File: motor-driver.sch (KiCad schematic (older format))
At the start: 9 parts, among them U3 A3950SLP-T

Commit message: Further work at PCB
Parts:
- R27, R28: footprint Resistor_SMD:R_0805_2012Metric_Pad1.15x1.40mm_HandSolder -> Resistor_SMD:R_0603_1608Metric_Pad1.05x0.95mm_HandSolder
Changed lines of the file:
@@
 AR Path="/5BF2FCBD/5BD9640D" Ref="U?"  Part="1"
 AR Path="/5C015BE4/5BD9640D" Ref="U5"  Part="1"
-F 0 "U3" H 6050 4415 50  0000 C CNN
+F 0 "U5" H 6050 4415 50  0000 C CNN
 F 1 "A3950SLP-T" H 6050 4324 50  0000 C CNN
 F 2 "Package_SO:HTSSOP-16-1EP_4.4x5mm_P0.65mm_EP3.4x5mm_Mask3x3mm_ThermalVias" H 6100 4300 50  0001 C CNN
@@
 AR Path="/5BF2FCBD/5BDA6B35" Ref="C?"  Part="1"
 AR Path="/5C015BE4/5BDA6B35" Ref="C16"  Part="1"
-F 0 "C7" H 6550 4400 50  0000 C CNN
+F 0 "C16" H 6550 4400 50  0000 C CNN
 F 1 "0.1uF 50V" H 6400 4300 50  0000 C CNN
 F 2 "Capacitor_SMD:C_0805_2012Metric_Pad1.15x1.40mm_HandSolder" H 6738 4200 50  0001 C CNN
@@
 AR Path="/5BF2FCBD/5BDBEA6E" Ref="C?"  Part="1"
 AR Path="/5C015BE4/5BDBEA6E" Ref="C20"  Part="1"
-F 0 "C11" V 7200 3750 50  0000 L CNN
+F 0 "C20" V 7200 3750 50  0000 L CNN
 F 1 "0.1uF 50V" V 7100 3600 50  0000 L CNN
 F 2 "Capacitor_SMD:C_0805_2012Metric_Pad1.15x1.40mm_HandSolder" H 7388 3650 50  0001 C CNN
@@
 AR Path="/5BF2FCBD/5BDD7CCD" Ref="C?"  Part="1"
 AR Path="/5C015BE4/5BDD7CCD" Ref="C17"  Part="1"
-F 0 "C8" V 6550 3350 50  0000 C CNN
+F 0 "C17" V 6550 3350 50  0000 C CNN
 F 1 "0.1uF 50V" V 6650 3350 50  0000 C CNN
 F 2 "Capacitor_SMD:C_0805_2012Metric_Pad1.15x1.40mm_HandSolder" H 6888 3200 50  0001 C CNN
@@
 AR Path="/5BF2FCBD/5BDE6995" Ref="C?"  Part="1"
 AR Path="/5C015BE4/5BDE6995" Ref="C18"  Part="1"
-F 0 "C9" H 7218 4396 50  0000 L CNN
+F 0 "C18" H 7218 4396 50  0000 L CNN
 F 1 "100uF" H 7218 4305 50  0000 L CNN
 F 2 "Capacitor_SMD:CP_Elec_8x10.5" H 7138 4200 50  0001 C CNN
@@
 AR Path="/5BF2FCBD/5BDFF4AF" Ref="C?"  Part="1"
 AR Path="/5C015BE4/5BDFF4AF" Ref="C19"  Part="1"
-F 0 "C10" V 7098 3200 50  0000 C CNN
+F 0 "C19" V 7098 3200 50  0000 C CNN
 F 1 "0.22uF 25V" V 7189 3200 50  0000 C CNN
 F 2 "Capacitor_SMD:C_0603_1608Metric_Pad1.05x0.95mm_HandSolder" H 7388 3050 50  0001 C CNN
@@
 AR Path="/5BF2FCBD/5BE2A012" Ref="R?"  Part="1"
 AR Path="/5C015BE4/5BE2A012" Ref="R44"  Part="1"
-F 0 "R27" H 5070 2846 50  0000 L CNN
+F 0 "R44" H 5070 2846 50  0000 L CNN
 F 1 "5k" H 5070 2755 50  0000 L CNN
-F 2 "Resistor_SMD:R_0805_2012Metric_Pad1.15x1.40mm_HandSolder" V 4930 2800 50  0001 C CNN
+F 2 "Resistor_SMD:R_0603_1608Metric_Pad1.05x0.95mm_HandSolder" V 4930 2800 50  0001 C CNN
 F 3 "~" H 5000 2800 50  0001 C CNN
 	1    5000 2800
@@
 AR Path="/5BF2FCBD/5BE427B2" Ref="D?"  Part="1"
 AR Path="/5C015BE4/5BE427B2" Ref="D8"  Part="1"
-F 0 "D5" V 5438 2282 50  0000 R CNN
+F 0 "D8" V 5438 2282 50  0000 R CNN
 F 1 "RED" V 5347 2282 50  0000 R CNN
 F 2 "LED_SMD:LED_0603_1608Metric_Pad1.05x0.95mm_HandSolder" H 5400 2400 50  0001 C CNN
@@
 AR Path="/5BF2FCBD/5BE42954" Ref="R?"  Part="1"
 AR Path="/5C015BE4/5BE42954" Ref="R45"  Part="1"
-F 0 "R28" H 5470 2846 50  0000 L CNN
+F 0 "R45" H 5470 2846 50  0000 L CNN
 F 1 "220" H 5470 2755 50  0000 L CNN
-F 2 "Resistor_SMD:R_0805_2012Metric_Pad1.15x1.40mm_HandSolder" V 5330 2800 50  0001 C CNN
+F 2 "Resistor_SMD:R_0603_1608Metric_Pad1.05x0.95mm_HandSolder" V 5330 2800 50  0001 C CNN
 F 3 "~" H 5400 2800 50  0001 C CNN
 	1    5400 2800

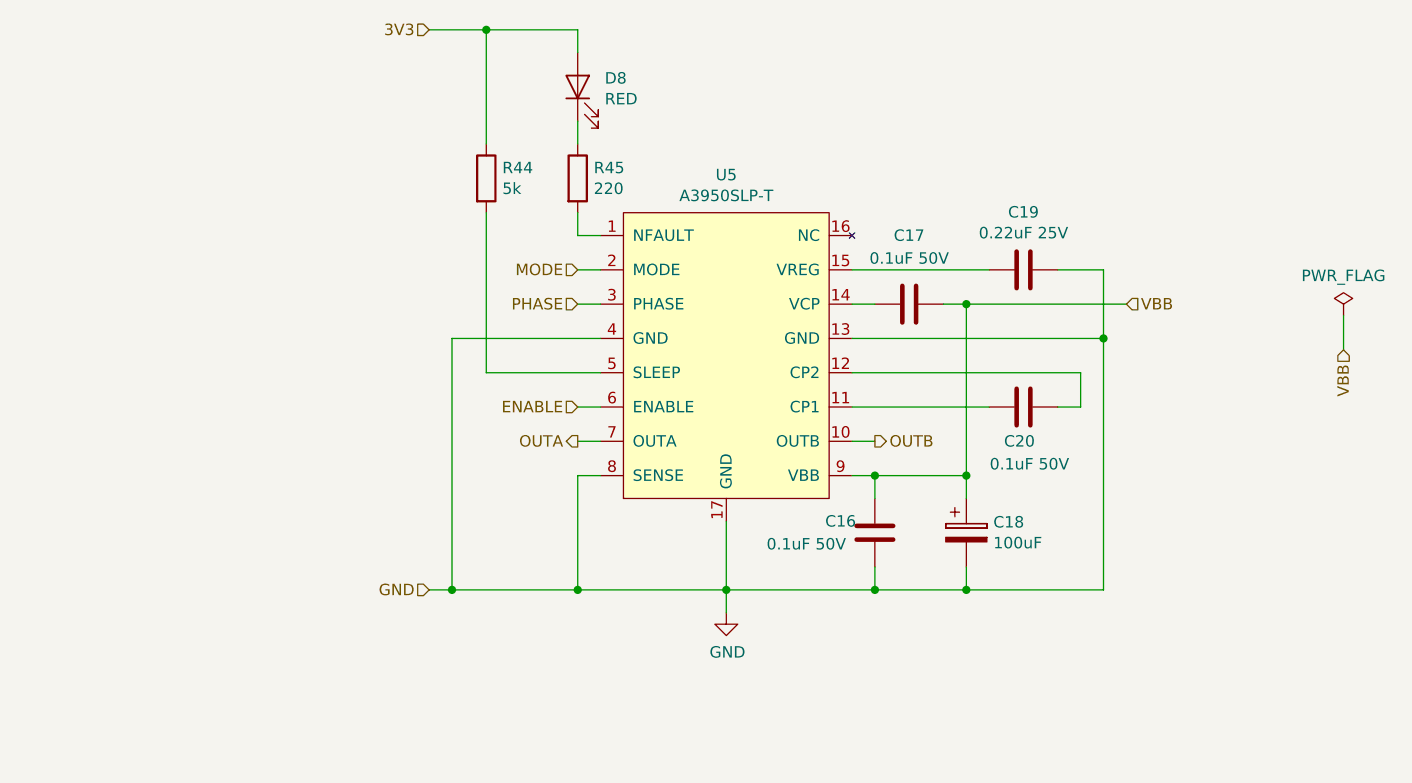
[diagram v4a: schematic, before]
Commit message: Changed Motor Controller to DRV8840, removed pre-motor power section. Replaced PNP transistors in logic level shifters with P-MOSFET units
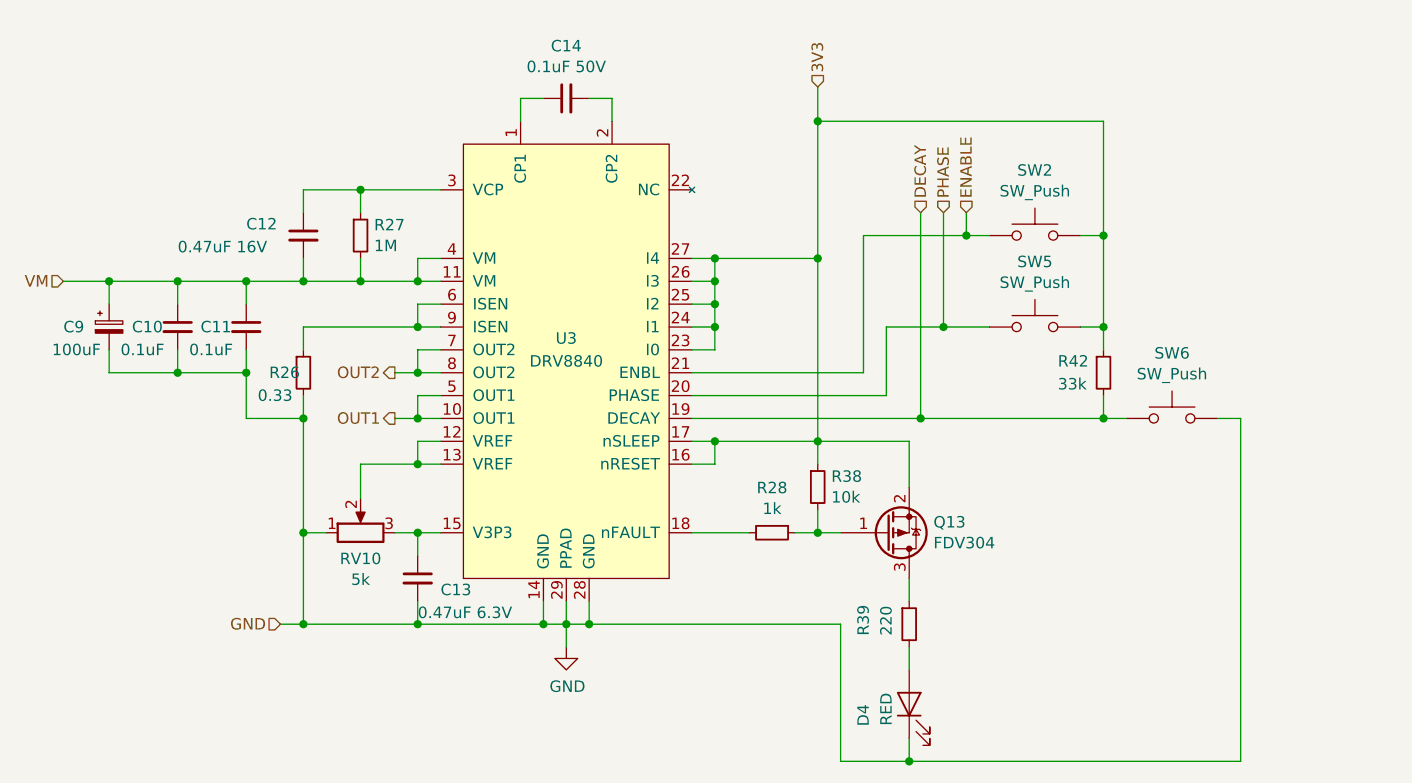
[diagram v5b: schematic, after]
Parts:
- removed C10: 0.22uF 25V, Capacitor_SMD:C_0603_1608Metric_Pad1.05x0.95mm_HandSolder, symbol Device:C
- removed C11, C7, C8: 0.1uF 50V, Capacitor_SMD:C_0805_2012Metric_Pad1.15x1.40mm_HandSolder, symbol Device:C
- removed C9: 100uF, Capacitor_SMD:CP_Elec_8x10.5, symbol Device:CP
- removed D5: RED, LED_SMD:LED_0603_1608Metric_Pad1.05x0.95mm_HandSolder, symbol Device:LED
- removed R27: 5k, Resistor_SMD:R_0603_1608Metric_Pad1.05x0.95mm_HandSolder, symbol Device:R
- removed R28: 220, Resistor_SMD:R_0603_1608Metric_Pad1.05x0.95mm_HandSolder, symbol Device:R
- removed U3: A3950SLP-T, Package_SO:HTSSOP-16-1EP_4.4x5mm_P0.65mm_EP3.4x5mm_Mask3x3mm_ThermalVias, symbol mylib:A3950SLP-T
- added C3: 100uF, Capacitor_SMD:CP_Elec_6.3x7.7, symbol Device:CP_Small
- added C4, C5: 0.1uF, Capacitor_SMD:C_0603_1608Metric, symbol Device:C_Small
- added C6: 0.47uF 16V, Capacitor_SMD:C_0603_1608Metric, symbol Device:C_Small
- added C7: 0.47uF 6.3V, Capacitor_SMD:C_0603_1608Metric, symbol Device:C_Small
- added C8: 0.1uF 50V, Capacitor_SMD:C_0603_1608Metric, symbol Device:C_Small
- added D3: RED, LED_SMD:LED_0603_1608Metric_Castellated, symbol Device:LED
- added Q13: FDV304, Package_TO_SOT_SMD:SOT-23, symbol Device:Q_PMOS_GSD
- added R21: 0.33, Resistor_SMD:R_2512_6332Metric, symbol Device:R_Small
- added R22: 1M, Resistor_SMD:R_0603_1608Metric, symbol Device:R_Small
- added R23: 1k, Resistor_SMD:R_0603_1608Metric, symbol Device:R_Small
- added R24: 10k, Resistor_SMD:R_0603_1608Metric, symbol Device:R_Small
- added R25: 220, Resistor_SMD:R_0603_1608Metric, symbol Device:R_Small
- added R41: 33k, Resistor_SMD:R_0603_1608Metric, symbol Device:R_Small
- added RV1: 5k, Potentiometer_THT:Potentiometer_Bourns_3266W_Vertical, symbol Device:R_POT
- added SW1, SW3, SW4: SW_Push, Button_Switch_SMD:SW_SPST_KMR2, symbol Switch:SW_Push
- added U2: DRV8840, SOP65P640X110-29N:SOP65P640X110-29N, symbol mylib:DRV8840
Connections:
- net 3V3: now also Q13.2 (S), R24.1, R41.1, SW1.2, SW3.2, U2.16 (nRESET), U2.17 (nSLEEP), U2.23 (I0), U2.24 (I1), U2.25 (I2), U2.26 (I3), U2.27 (I4)
- net ENABLE: now also SW1.1, U2.21 (ENBL)
- net GND: now also C3.2, C4.2, C5.2, C7.2, D3.1 (K), R21.2, RV1.1, SW4.2, U2.14 (GND), U2.28 (GND), U2.29 (PPAD)
- net PHASE: now also SW3.1, U2.20 (PHASE)
- new net: C8.1, U2.1 (CP1)
- new net: RV1.2, U2.12 (VREF), U2.13 (VREF)
- new net: C7.1, RV1.3, U2.15 (V3P3)
- new net: R23.2, U2.18 (nFAULT)
- new net: C8.2, U2.2 (CP2)
- new net: C6.1, R22.1, U2.3 (VCP)
- new net: R21.1, U2.6 (ISEN), U2.9 (ISEN)
- new net: Q13.1 (G), R23.1, R24.2
- new net: D3.2 (A), R25.2
- new net: Q13.3 (D), R25.1
- new net DECAY: R41.2, SW4.1, U2.19 (DECAY)
- new net OUT1: U2.10 (OUT1), U2.5 (OUT1)
- new net OUT2: U2.7 (OUT2), U2.8 (OUT2)
- new net VM: C3.1, C4.1, C5.1, C6.2, R22.2, U2.11 (VM), U2.4 (VM)

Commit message: Re-placed components of 3.3->24V converter. Improvement placement of Motor Controller components
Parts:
- C3: footprint Capacitor_SMD:CP_Elec_6.3x7.7 -> Capacitor_THT:CP_Radial_D6.3mm_P2.50mm
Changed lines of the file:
@@
 F 0 "C9" H 3150 3450 50  0000 L CNN
 F 1 "100uF" H 3100 3350 50  0000 L CNN
-F 2 "Capacitor_SMD:CP_Elec_6.3x7.7" H 3350 3450 50  0001 C CNN
+F 2 "Capacitor_THT:CP_Radial_D6.3mm_P2.50mm" H 3350 3450 50  0001 C CNN
 F 3 "~" H 3350 3450 50  0001 C CNN
 	1    3350 3450

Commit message: Routed all nets without GND. Added logo
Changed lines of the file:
@@
 $Descr A4 11693 8268
 encoding utf-8
-Sheet 7 8
+Sheet 5 8
 Title ""
 Date ""
@@
 AR Path="/5BDB64FF/5BE79BC7" Ref="R22"  Part="1"
 AR Path="/5C015BE4/5BE79BC7" Ref="R27"  Part="1"
-F 0 "R27" H 4509 3096 50  0000 L CNN
+F 0 "R22" H 4509 3096 50  0000 L CNN
 F 1 "1M" H 4509 3005 50  0000 L CNN
 F 2 "Resistor_SMD:R_0603_1608Metric" H 4450 3050 50  0001 C CNN
@@
 AR Path="/5BDB64FF/5BE79D59" Ref="C8"  Part="1"
 AR Path="/5C015BE4/5BE79D59" Ref="C14"  Part="1"
-F 0 "C14" V 5579 2450 50  0000 C CNN
+F 0 "C8" V 5579 2450 50  0000 C CNN
 F 1 "0.1uF 50V" V 5488 2450 50  0000 C CNN
 F 2 "Capacitor_SMD:C_0603_1608Metric" H 5350 2450 50  0001 C CNN
@@
 AR Path="/5BDB64FF/5BE7C590" Ref="C6"  Part="1"
 AR Path="/5C015BE4/5BE7C590" Ref="C12"  Part="1"
-F 0 "C12" H 3950 3100 50  0000 L CNN
+F 0 "C6" H 3950 3100 50  0000 L CNN
 F 1 "0.47uF 16V" H 3650 3000 50  0000 L CNN
 F 2 "Capacitor_SMD:C_0603_1608Metric" H 4200 3050 50  0001 C CNN
@@
 AR Path="/5BDB64FF/5BE78B4F" Ref="U2"  Part="1"
 AR Path="/5C015BE4/5BE78B4F" Ref="U3"  Part="1"
-F 0 "U3" H 5350 3700 50  0000 C CNN
+F 0 "U2" H 5350 3700 50  0000 C CNN
 F 1 "DRV8840" H 5350 3600 50  0000 C CNN
 F 2 "SOP65P640X110-29N:SOP65P640X110-29N" H 5200 3700 50  0001 C CNN
@@
 AR Path="/5BDB64FF/5BE7DEED" Ref="C5"  Part="1"
 AR Path="/5C015BE4/5BE7DEED" Ref="C11"  Part="1"
-F 0 "C11" H 3750 3450 50  0000 L CNN
+F 0 "C5" H 3750 3450 50  0000 L CNN
 F 1 "0.1uF" H 3700 3350 50  0000 L CNN
 F 2 "Capacitor_SMD:C_0603_1608Metric" H 3950 3450 50  0001 C CNN
@@
 AR Path="/5BDB64FF/5BE7DF37" Ref="C4"  Part="1"
 AR Path="/5C015BE4/5BE7DF37" Ref="C10"  Part="1"
-F 0 "C10" H 3450 3450 50  0000 L CNN
+F 0 "C4" H 3450 3450 50  0000 L CNN
 F 1 "0.1uF" H 3400 3350 50  0000 L CNN
 F 2 "Capacitor_SMD:C_0603_1608Metric" H 3650 3450 50  0001 C CNN
@@
 AR Path="/5BDB64FF/5BE7EFAF" Ref="C3"  Part="1"
 AR Path="/5C015BE4/5BE7EFAF" Ref="C9"  Part="1"
-F 0 "C9" H 3150 3450 50  0000 L CNN
+F 0 "C3" H 3150 3450 50  0000 L CNN
 F 1 "100uF" H 3100 3350 50  0000 L CNN
 F 2 "Capacitor_THT:CP_Radial_D6.3mm_P2.50mm" H 3350 3450 50  0001 C CNN
@@
 AR Path="/5BDB64FF/5BE7F85E" Ref="#PWR05"  Part="1"
 AR Path="/5C015BE4/5BE7F85E" Ref="#PWR07"  Part="1"
-F 0 "#PWR07" H 5350 4600 50  0001 C CNN
+F 0 "#PWR05" H 5350 4600 50  0001 C CNN
 F 1 "GND" H 5355 4677 50  0000 C CNN
 F 2 "" H 5350 4850 50  0001 C CNN
@@
 AR Path="/5BDB64FF/5BE84287" Ref="R21"  Part="1"
 AR Path="/5C015BE4/5BE84287" Ref="R26"  Part="1"
-F 0 "R26" H 4050 3650 50  0000 L CNN
+F 0 "R21" H 4050 3650 50  0000 L CNN
 F 1 "0.33" H 4000 3550 50  0000 L CNN
 F 2 "Resistor_SMD:R_2512_6332Metric" H 4200 3650 50  0001 C CNN
@@
 AR Path="/5BDB64FF/5BEAA7B3" Ref="R24"  Part="1"
 AR Path="/5C015BE4/5BEAA7B3" Ref="R38"  Part="1"
-F 0 "R38" H 6509 4196 50  0000 L CNN
+F 0 "R24" H 6509 4196 50  0000 L CNN
 F 1 "10k" H 6509 4105 50  0000 L CNN
 F 2 "Resistor_SMD:R_0603_1608Metric" H 6450 4150 50  0001 C CNN
@@
 AR Path="/5BDB64FF/5BEAD7B9" Ref="R23"  Part="1"
 AR Path="/5C015BE4/5BEAD7B9" Ref="R28"  Part="1"
-F 0 "R28" V 6054 4350 50  0000 C CNN
+F 0 "R23" V 6054 4350 50  0000 C CNN
 F 1 "1k" V 6145 4350 50  0000 C CNN
 F 2 "Resistor_SMD:R_0603_1608Metric" H 6250 4350 50  0001 C CNN
@@
 AR Path="/5BDB64FF/5BEB256D" Ref="D3"  Part="1"
 AR Path="/5C015BE4/5BEB256D" Ref="D4"  Part="1"
-F 0 "D4" H 6850 5300 50  0000 R CNN
+F 0 "D3" H 6850 5300 50  0000 R CNN
 F 1 "RED" H 6900 5200 50  0000 R CNN
 F 2 "LED_SMD:LED_0603_1608Metric_Castellated" H 6850 5100 50  0001 C CNN
@@
 AR Path="/5BDB64FF/5BEB7620" Ref="R25"  Part="1"
 AR Path="/5C015BE4/5BEB7620" Ref="R39"  Part="1"
-F 0 "R39" V 6650 4700 50  0000 L CNN
+F 0 "R25" V 6650 4700 50  0000 L CNN
 F 1 "220" V 6750 4700 50  0000 L CNN
 F 2 "Resistor_SMD:R_0603_1608Metric" H 6850 4750 50  0001 C CNN
@@
 AR Path="/5BDB64FF/5BECAFEA" Ref="C7"  Part="1"
 AR Path="/5C015BE4/5BECAFEA" Ref="C13"  Part="1"
-F 0 "C13" H 4800 4500 50  0000 L CNN
+F 0 "C7" H 4800 4500 50  0000 L CNN
 F 1 "0.47uF 6.3V" H 4700 4400 50  0000 L CNN
 F 2 "Capacitor_SMD:C_0603_1608Metric" H 4700 4550 50  0001 C CNN
@@
 AR Path="/5BDB64FF/5BE92513" Ref="RV1"  Part="1"
 AR Path="/5C015BE4/5BE92513" Ref="RV10"  Part="1"
-F 0 "RV10" V 4336 4350 50  0000 C CNN
+F 0 "RV1" V 4336 4350 50  0000 C CNN
 F 1 "5k" V 4245 4350 50  0000 C CNN
 F 2 "Potentiometer_THT:Potentiometer_Bourns_3266W_Vertical" H 4450 4350 50  0001 C CNN
@@
 AR Path="/5C015BE4/5BF252CB" Ref="Q13"  Part="1"
 AR Path="/5BDB64FF/5BF252CB" Ref="Q9"  Part="1"
-F 0 "Q13" H 6956 4304 50  0000 L CNN
+F 0 "Q9" H 6956 4304 50  0000 L CNN
 F 1 "FDV304" H 6956 4395 50  0000 L CNN
 F 2 "Package_TO_SOT_SMD:SOT-23" H 6950 4450 50  0001 C CNN
@@
 AR Path="/5BDB64FF/5BE949DE" Ref="SW1"  Part="1"
 AR Path="/5C015BE4/5BE949DE" Ref="SW2"  Part="1"
-F 0 "SW2" H 7400 3335 50  0000 C CNN
+F 0 "SW1" H 7400 3335 50  0000 C CNN
 F 1 "SW_Push" H 7400 3244 50  0000 C CNN
 F 2 "Button_Switch_SMD:SW_SPST_KMR2" H 7400 3250 50  0001 C CNN
@@
 AR Path="/5BDB64FF/5BE950B7" Ref="SW3"  Part="1"
 AR Path="/5C015BE4/5BE950B7" Ref="SW5"  Part="1"
-F 0 "SW5" H 7400 3735 50  0000 C CNN
+F 0 "SW3" H 7400 3735 50  0000 C CNN
 F 1 "SW_Push" H 7400 3644 50  0000 C CNN
 F 2 "Button_Switch_SMD:SW_SPST_KMR2" H 7400 3650 50  0001 C CNN
@@
 AR Path="/5BDB64FF/5BE950FD" Ref="SW4"  Part="1"
 AR Path="/5C015BE4/5BE950FD" Ref="SW6"  Part="1"
-F 0 "SW6" H 8000 4135 50  0000 C CNN
+F 0 "SW4" H 8000 4135 50  0000 C CNN
 F 1 "SW_Push" H 8000 4044 50  0000 C CNN
 F 2 "Button_Switch_SMD:SW_SPST_KMR2" H 8000 4050 50  0001 C CNN
@@
 AR Path="/5BDB64FF/5BEB4B1E" Ref="R41"  Part="1"
 AR Path="/5C015BE4/5BEB4B1E" Ref="R42"  Part="1"
-F 0 "R42" H 7500 3700 50  0000 L CNN
+F 0 "R41" H 7500 3700 50  0000 L CNN
 F 1 "33k" H 7500 3600 50  0000 L CNN
 F 2 "Resistor_SMD:R_0603_1608Metric" H 7700 3650 50  0001 C CNN

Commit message: Added switch for selecting Low/High power motor. Added thermal pads around motor controllers.
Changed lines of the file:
@@
 $Descr A4 11693 8268
 encoding utf-8
-Sheet 5 8
+Sheet 7 8
 Title ""
 Date ""
@@
 AR Path="/5BDB64FF/5BE79BC7" Ref="R22"  Part="1"
 AR Path="/5C015BE4/5BE79BC7" Ref="R27"  Part="1"
-F 0 "R22" H 4509 3096 50  0000 L CNN
+F 0 "R27" H 4509 3096 50  0000 L CNN
 F 1 "1M" H 4509 3005 50  0000 L CNN
 F 2 "Resistor_SMD:R_0603_1608Metric" H 4450 3050 50  0001 C CNN
@@
 AR Path="/5BDB64FF/5BE79D59" Ref="C8"  Part="1"
 AR Path="/5C015BE4/5BE79D59" Ref="C14"  Part="1"
-F 0 "C8" V 5579 2450 50  0000 C CNN
+F 0 "C14" V 5579 2450 50  0000 C CNN
 F 1 "0.1uF 50V" V 5488 2450 50  0000 C CNN
 F 2 "Capacitor_SMD:C_0603_1608Metric" H 5350 2450 50  0001 C CNN
@@
 AR Path="/5BDB64FF/5BE7C590" Ref="C6"  Part="1"
 AR Path="/5C015BE4/5BE7C590" Ref="C12"  Part="1"
-F 0 "C6" H 3950 3100 50  0000 L CNN
+F 0 "C12" H 3950 3100 50  0000 L CNN
 F 1 "0.47uF 16V" H 3650 3000 50  0000 L CNN
 F 2 "Capacitor_SMD:C_0603_1608Metric" H 4200 3050 50  0001 C CNN
@@
 AR Path="/5BDB64FF/5BE78B4F" Ref="U2"  Part="1"
 AR Path="/5C015BE4/5BE78B4F" Ref="U3"  Part="1"
-F 0 "U2" H 5350 3700 50  0000 C CNN
+F 0 "U3" H 5350 3700 50  0000 C CNN
 F 1 "DRV8840" H 5350 3600 50  0000 C CNN
 F 2 "SOP65P640X110-29N:SOP65P640X110-29N" H 5200 3700 50  0001 C CNN
@@
 AR Path="/5BDB64FF/5BE7DEED" Ref="C5"  Part="1"
 AR Path="/5C015BE4/5BE7DEED" Ref="C11"  Part="1"
-F 0 "C5" H 3750 3450 50  0000 L CNN
+F 0 "C11" H 3750 3450 50  0000 L CNN
 F 1 "0.1uF" H 3700 3350 50  0000 L CNN
 F 2 "Capacitor_SMD:C_0603_1608Metric" H 3950 3450 50  0001 C CNN
@@
 AR Path="/5BDB64FF/5BE7DF37" Ref="C4"  Part="1"
 AR Path="/5C015BE4/5BE7DF37" Ref="C10"  Part="1"
-F 0 "C4" H 3450 3450 50  0000 L CNN
+F 0 "C10" H 3450 3450 50  0000 L CNN
 F 1 "0.1uF" H 3400 3350 50  0000 L CNN
 F 2 "Capacitor_SMD:C_0603_1608Metric" H 3650 3450 50  0001 C CNN
@@
 AR Path="/5BDB64FF/5BE7EFAF" Ref="C3"  Part="1"
 AR Path="/5C015BE4/5BE7EFAF" Ref="C9"  Part="1"
-F 0 "C3" H 3150 3450 50  0000 L CNN
+F 0 "C9" H 3150 3450 50  0000 L CNN
 F 1 "100uF" H 3100 3350 50  0000 L CNN
 F 2 "Capacitor_THT:CP_Radial_D6.3mm_P2.50mm" H 3350 3450 50  0001 C CNN
@@
 AR Path="/5BDB64FF/5BE7F85E" Ref="#PWR05"  Part="1"
 AR Path="/5C015BE4/5BE7F85E" Ref="#PWR07"  Part="1"
-F 0 "#PWR05" H 5350 4600 50  0001 C CNN
+F 0 "#PWR07" H 5350 4600 50  0001 C CNN
 F 1 "GND" H 5355 4677 50  0000 C CNN
 F 2 "" H 5350 4850 50  0001 C CNN
@@
 AR Path="/5BDB64FF/5BE84287" Ref="R21"  Part="1"
 AR Path="/5C015BE4/5BE84287" Ref="R26"  Part="1"
-F 0 "R21" H 4050 3650 50  0000 L CNN
+F 0 "R26" H 4050 3650 50  0000 L CNN
 F 1 "0.33" H 4000 3550 50  0000 L CNN
 F 2 "Resistor_SMD:R_2512_6332Metric" H 4200 3650 50  0001 C CNN
@@
 AR Path="/5BDB64FF/5BEAA7B3" Ref="R24"  Part="1"
 AR Path="/5C015BE4/5BEAA7B3" Ref="R38"  Part="1"
-F 0 "R24" H 6509 4196 50  0000 L CNN
+F 0 "R38" H 6509 4196 50  0000 L CNN
 F 1 "10k" H 6509 4105 50  0000 L CNN
 F 2 "Resistor_SMD:R_0603_1608Metric" H 6450 4150 50  0001 C CNN
@@
 AR Path="/5BDB64FF/5BEAD7B9" Ref="R23"  Part="1"
 AR Path="/5C015BE4/5BEAD7B9" Ref="R28"  Part="1"
-F 0 "R23" V 6054 4350 50  0000 C CNN
+F 0 "R28" V 6054 4350 50  0000 C CNN
 F 1 "1k" V 6145 4350 50  0000 C CNN
 F 2 "Resistor_SMD:R_0603_1608Metric" H 6250 4350 50  0001 C CNN
@@
 AR Path="/5BDB64FF/5BEB256D" Ref="D3"  Part="1"
 AR Path="/5C015BE4/5BEB256D" Ref="D4"  Part="1"
-F 0 "D3" H 6850 5300 50  0000 R CNN
+F 0 "D4" H 6850 5300 50  0000 R CNN
 F 1 "RED" H 6900 5200 50  0000 R CNN
 F 2 "LED_SMD:LED_0603_1608Metric_Castellated" H 6850 5100 50  0001 C CNN
@@
 AR Path="/5BDB64FF/5BEB7620" Ref="R25"  Part="1"
 AR Path="/5C015BE4/5BEB7620" Ref="R39"  Part="1"
-F 0 "R25" V 6650 4700 50  0000 L CNN
+F 0 "R39" V 6650 4700 50  0000 L CNN
 F 1 "220" V 6750 4700 50  0000 L CNN
 F 2 "Resistor_SMD:R_0603_1608Metric" H 6850 4750 50  0001 C CNN
@@
 AR Path="/5BDB64FF/5BECAFEA" Ref="C7"  Part="1"
 AR Path="/5C015BE4/5BECAFEA" Ref="C13"  Part="1"
-F 0 "C7" H 4800 4500 50  0000 L CNN
+F 0 "C13" H 4800 4500 50  0000 L CNN
 F 1 "0.47uF 6.3V" H 4700 4400 50  0000 L CNN
 F 2 "Capacitor_SMD:C_0603_1608Metric" H 4700 4550 50  0001 C CNN
@@
 AR Path="/5BDB64FF/5BE92513" Ref="RV1"  Part="1"
 AR Path="/5C015BE4/5BE92513" Ref="RV10"  Part="1"
-F 0 "RV1" V 4336 4350 50  0000 C CNN
+F 0 "RV10" V 4336 4350 50  0000 C CNN
 F 1 "5k" V 4245 4350 50  0000 C CNN
 F 2 "Potentiometer_THT:Potentiometer_Bourns_3266W_Vertical" H 4450 4350 50  0001 C CNN
@@
 AR Path="/5C015BE4/5BF252CB" Ref="Q13"  Part="1"
 AR Path="/5BDB64FF/5BF252CB" Ref="Q9"  Part="1"
-F 0 "Q9" H 6956 4304 50  0000 L CNN
+F 0 "Q13" H 6956 4304 50  0000 L CNN
 F 1 "FDV304" H 6956 4395 50  0000 L CNN
 F 2 "Package_TO_SOT_SMD:SOT-23" H 6950 4450 50  0001 C CNN
@@
 AR Path="/5BDB64FF/5BE949DE" Ref="SW1"  Part="1"
 AR Path="/5C015BE4/5BE949DE" Ref="SW2"  Part="1"
-F 0 "SW1" H 7400 3335 50  0000 C CNN
+F 0 "SW2" H 7400 3335 50  0000 C CNN
 F 1 "SW_Push" H 7400 3244 50  0000 C CNN
 F 2 "Button_Switch_SMD:SW_SPST_KMR2" H 7400 3250 50  0001 C CNN
@@
 AR Path="/5BDB64FF/5BE950B7" Ref="SW3"  Part="1"
 AR Path="/5C015BE4/5BE950B7" Ref="SW5"  Part="1"
-F 0 "SW3" H 7400 3735 50  0000 C CNN
+F 0 "SW5" H 7400 3735 50  0000 C CNN
 F 1 "SW_Push" H 7400 3644 50  0000 C CNN
 F 2 "Button_Switch_SMD:SW_SPST_KMR2" H 7400 3650 50  0001 C CNN
@@
 AR Path="/5BDB64FF/5BE950FD" Ref="SW4"  Part="1"
 AR Path="/5C015BE4/5BE950FD" Ref="SW6"  Part="1"
-F 0 "SW4" H 8000 4135 50  0000 C CNN
+F 0 "SW6" H 8000 4135 50  0000 C CNN
 F 1 "SW_Push" H 8000 4044 50  0000 C CNN
 F 2 "Button_Switch_SMD:SW_SPST_KMR2" H 8000 4050 50  0001 C CNN
@@
 AR Path="/5BDB64FF/5BEB4B1E" Ref="R41"  Part="1"
 AR Path="/5C015BE4/5BEB4B1E" Ref="R42"  Part="1"
-F 0 "R41" H 7500 3700 50  0000 L CNN
+F 0 "R42" H 7500 3700 50  0000 L CNN
 F 1 "33k" H 7500 3600 50  0000 L CNN
 F 2 "Resistor_SMD:R_0603_1608Metric" H 7700 3650 50  0001 C CNN
